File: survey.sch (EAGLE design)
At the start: 11 parts, among them IC1 DS1820, J1 PJ-102AH

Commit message: add receiver's shematic
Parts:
- renumbered IC1 to TSENSOR, J1 to SOCKET, JP1 to USB, U1 to ESP-12E
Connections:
- net GND: now also ESP-12E.GPIO0, ESP-12E.GPIO15
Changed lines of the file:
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@@
 </classes>
 <parts>
-<part name="U1" library="esp8266modules" deviceset="ESP12E" device="SMD"/>
-<part name="IC1" library="DS1820" deviceset="DS1820" device=""/>
+<part name="ESP-12E" library="esp8266modules" deviceset="ESP12E" device="SMD"/>
+<part name="TSENSOR" library="DS1820" deviceset="DS1820" device=""/>
 <part name="GND1" library="supply1" library_urn="urn:adsk.eagle:library:371" deviceset="GND" device=""/>
 <part name="SUPPLY1" library="supply2" library_urn="urn:adsk.eagle:library:372" deviceset="VCC" device=""/>
-<part name="JP1" library="pinhead" library_urn="urn:adsk.eagle:library:325" deviceset="PINHD-1X4" device="" package3d_urn="urn:adsk.eagle:package:22407/2"/>
+<part name="USB" library="pinhead" library_urn="urn:adsk.eagle:library:325" deviceset="PINHD-1X4" device="" package3d_urn="urn:adsk.eagle:package:22407/2"/>
 <part name="SUPPLY2" library="supply2" library_urn="urn:adsk.eagle:library:372" deviceset="VCC" device=""/>
 <part name="GND2" library="supply1" library_urn="urn:adsk.eagle:library:371" deviceset="GND" device=""/>
 <part name="GND3" library="supply1" library_urn="urn:adsk.eagle:library:371" deviceset="GND" device=""/>
-<part name="J1" library="connector" deviceset="PJ-102AH" device=""/>
+<part name="SOCKET" library="connector" deviceset="PJ-102AH" device=""/>
 <part name="GND4" library="supply1" library_urn="urn:adsk.eagle:library:371" deviceset="GND" device=""/>
 <part name="C1" library="rcl" library_urn="urn:adsk.eagle:library:334" deviceset="CPOL-EU" device="E2.5-6" package3d_urn="urn:adsk.eagle:package:23349/1"/>
@@
 <part name="H3" library="holes" library_urn="urn:adsk.eagle:library:237" deviceset="MOUNT-HOLE" device="3.0" package3d_urn="urn:adsk.eagle:package:14277/1"/>
 <part name="H4" library="holes" library_urn="urn:adsk.eagle:library:237" deviceset="MOUNT-HOLE" device="3.0" package3d_urn="urn:adsk.eagle:package:14277/1"/>
+<part name="GND6" library="supply1" library_urn="urn:adsk.eagle:library:371" deviceset="GND" device=""/>
+<part name="GND7" library="supply1" library_urn="urn:adsk.eagle:library:371" deviceset="GND" device=""/>
 </parts>
 <sheets>
@@
 </plain>
 <instances>
-<instance part="U1" gate="G$1" x="55.88" y="78.74"/>
-<instance part="IC1" gate="G$1" x="116.84" y="83.82"/>
+<instance part="ESP-12E" gate="G$1" x="55.88" y="78.74"/>
+<instance part="TSENSOR" gate="G$1" x="116.84" y="83.82"/>
 <instance part="GND1" gate="1" x="116.84" y="71.12"/>
 <instance part="SUPPLY1" gate="G$1" x="96.52" y="88.9"/>
-<instance part="JP1" gate="A" x="88.9" y="96.52"/>
+<instance part="USB" gate="A" x="88.9" y="96.52"/>
 <instance part="SUPPLY2" gate="G$1" x="76.2" y="106.68"/>
 <instance part="GND2" gate="1" x="78.74" y="88.9"/>
 <instance part="GND3" gate="1" x="78.74" y="66.04"/>
-<instance part="J1" gate="G$1" x="-2.54" y="109.22"/>
+<instance part="SOCKET" gate="G$1" x="-2.54" y="109.22"/>
 <instance part="GND4" gate="1" x="7.62" y="101.6"/>
 <instance part="C1" gate="G$1" x="15.24" y="109.22"/>
@@
 <instance part="H3" gate="G$1" x="111.76" y="114.3"/>
 <instance part="H4" gate="G$1" x="99.06" y="114.3"/>
+<instance part="GND6" gate="1" x="83.82" y="76.2"/>
+<instance part="GND7" gate="1" x="88.9" y="63.5"/>
 </instances>
 <busses>
@@
 <net name="N$1" class="0">
 <segment>
-<pinref part="IC1" gate="G$1" pin="DQ"/>
+<pinref part="TSENSOR" gate="G$1" pin="DQ"/>
 <wire x1="127" y1="86.36" x2="127" y2="66.04" width="0.1524" layer="91"/>
-<pinref part="U1" gate="G$1" pin="GPIO2"/>
+<pinref part="ESP-12E" gate="G$1" pin="GPIO2"/>
 <wire x1="71.12" y1="73.66" x2="96.52" y2="73.66" width="0.1524" layer="91"/>
 <wire x1="96.52" y1="73.66" x2="96.52" y2="66.04" width="0.1524" layer="91"/>
@@
 <segment>
 <pinref part="SUPPLY1" gate="G$1" pin="VCC"/>
-<pinref part="IC1" gate="G$1" pin="VDD"/>
+<pinref part="TSENSOR" gate="G$1" pin="VDD"/>
 <wire x1="96.52" y1="86.36" x2="106.68" y2="86.36" width="0.1524" layer="91"/>
 </segment>
 <segment>
-<pinref part="JP1" gate="A" pin="1"/>
+<pinref part="USB" gate="A" pin="1"/>
 <wire x1="86.36" y1="101.6" x2="76.2" y2="101.6" width="0.1524" layer="91"/>
 <wire x1="76.2" y1="101.6" x2="76.2" y2="104.14" width="0.1524" layer="91"/>
@@
 </segment>
 <segment>
-<pinref part="J1" gate="G$1" pin="VCC"/>
+<pinref part="SOCKET" gate="G$1" pin="VCC"/>
 <wire x1="5.08" y1="111.76" x2="15.24" y2="111.76" width="0.1524" layer="91"/>
 <pinref part="C1" gate="G$1" pin="+"/>
@@
 <segment>
 <pinref part="SUPPLY4" gate="G$1" pin="VCC"/>
-<pinref part="U1" gate="G$1" pin="VCC"/>
+<pinref part="ESP-12E" gate="G$1" pin="VCC"/>
 <wire x1="22.86" y1="68.58" x2="38.1" y2="68.58" width="0.1524" layer="91"/>
 </segment>
@@
 <segment>
 <pinref part="GND1" gate="1" pin="GND"/>
-<pinref part="IC1" gate="G$1" pin="GND"/>
+<pinref part="TSENSOR" gate="G$1" pin="GND"/>
 <wire x1="116.84" y1="73.66" x2="116.84" y2="76.2" width="0.1524" layer="91"/>
 </segment>
 <segment>
-<pinref part="JP1" gate="A" pin="4"/>
+<pinref part="USB" gate="A" pin="4"/>
 <wire x1="86.36" y1="93.98" x2="78.74" y2="93.98" width="0.1524" layer="91"/>
 <wire x1="78.74" y1="93.98" x2="78.74" y2="91.44" width="0.1524" layer="91"/>
@@
 </segment>
 <segment>
-<pinref part="U1" gate="G$1" pin="GND"/>
+<pinref part="ESP-12E" gate="G$1" pin="GND"/>
 <pinref part="GND3" gate="1" pin="GND"/>
 <wire x1="71.12" y1="68.58" x2="78.74" y2="68.58" width="0.1524" layer="91"/>
 </segment>
 <segment>
-<pinref part="J1" gate="G$1" pin="GND"/>
+<pinref part="SOCKET" gate="G$1" pin="GND"/>
 <wire x1="5.08" y1="106.68" x2="7.62" y2="106.68" width="0.1524" layer="91"/>
 <pinref part="GND4" gate="1" pin="GND"/>
@@
 <pinref part="GND5" gate="1" pin="GND"/>
 </segment>
+<segment>
+<pinref part="ESP-12E" gate="G$1" pin="GPIO0"/>
+<wire x1="71.12" y1="76.2" x2="78.74" y2="76.2" width="0.1524" layer="91"/>
+<wire x1="78.74" y1="76.2" x2="78.74" y2="81.28" width="0.1524" layer="91"/>
+<wire x1="78.74" y1="81.28" x2="83.82" y2="81.28" width="0.1524" layer="91"/>
+<pinref part="GND6" gate="1" pin="GND"/>
+<wire x1="83.82" y1="81.28" x2="83.82" y2="78.74" width="0.1524" layer="91"/>
+</segment>
+<segment>
+<pinref part="GND7" gate="1" pin="GND"/>
+<wire x1="88.9" y1="66.04" x2="88.9" y2="71.12" width="0.1524" layer="91"/>
+<pinref part="ESP-12E" gate="G$1" pin="GPIO15"/>
+<wire x1="88.9" y1="71.12" x2="71.12" y2="71.12" width="0.1524" layer="91"/>
+</segment>
 </net>
 <net name="N$3" class="0">
 <segment>
-<pinref part="U1" gate="G$1" pin="TX"/>
+<pinref part="ESP-12E" gate="G$1" pin="TX"/>
 <wire x1="71.12" y1="86.36" x2="73.66" y2="86.36" width="0.1524" layer="91"/>
 <wire x1="73.66" y1="86.36" x2="73.66" y2="99.06" width="0.1524" layer="91"/>
-<pinref part="JP1" gate="A" pin="2"/>
+<pinref part="USB" gate="A" pin="2"/>
 <wire x1="73.66" y1="99.06" x2="86.36" y2="99.06" width="0.1524" layer="91"/>
 </segment>
@@
 <net name="N$4" class="0">
 <segment>
-<pinref part="U1" gate="G$1" pin="RX"/>
+<pinref part="ESP-12E" gate="G$1" pin="RX"/>
 <wire x1="71.12" y1="83.82" x2="76.2" y2="83.82" width="0.1524" layer="91"/>
 <wire x1="76.2" y1="83.82" x2="76.2" y2="96.52" width="0.1524" layer="91"/>
-<pinref part="JP1" gate="A" pin="3"/>
+<pinref part="USB" gate="A" pin="3"/>
 <wire x1="76.2" y1="96.52" x2="86.36" y2="96.52" width="0.1524" layer="91"/>
 </segment>
@@
 <wire x1="30.48" y1="81.28" x2="33.02" y2="81.28" width="0.1524" layer="91"/>
 <wire x1="33.02" y1="81.28" x2="33.02" y2="86.36" width="0.1524" layer="91"/>
-<pinref part="U1" gate="G$1" pin="RESET"/>
+<pinref part="ESP-12E" gate="G$1" pin="RESET"/>
 <wire x1="33.02" y1="86.36" x2="38.1" y2="86.36" width="0.1524" layer="91"/>
-<pinref part="U1" gate="G$1" pin="CH_PD"/>
+<pinref part="ESP-12E" gate="G$1" pin="CH_PD"/>
 <wire x1="33.02" y1="81.28" x2="38.1" y2="81.28" width="0.1524" layer="91"/>
 <junction x="33.02" y="81.28"/>

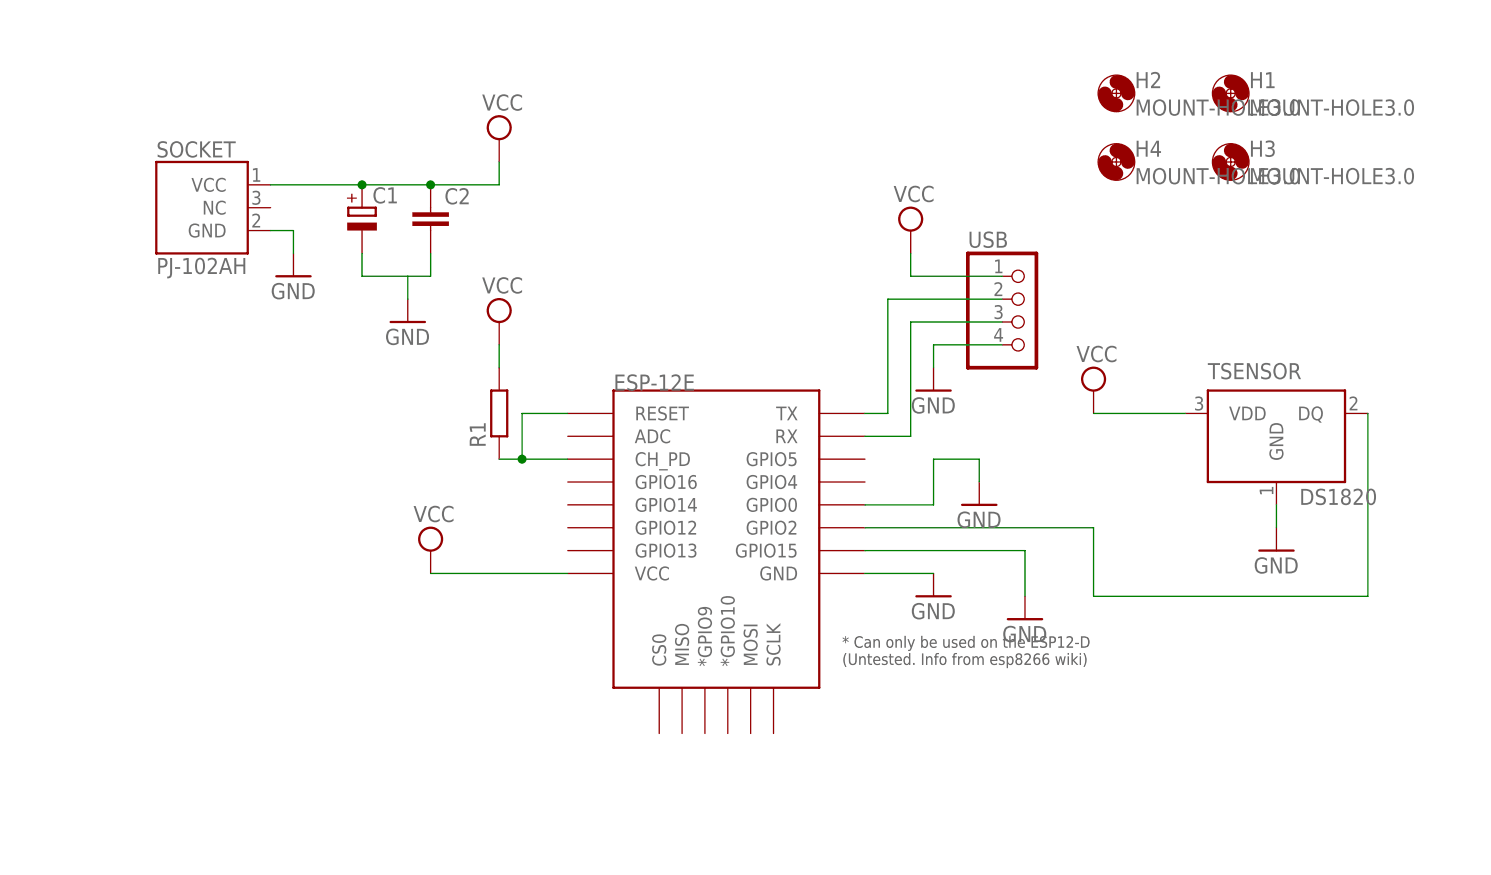
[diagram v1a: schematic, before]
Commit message: Improved some bugs in receiver's and survey's schematic.
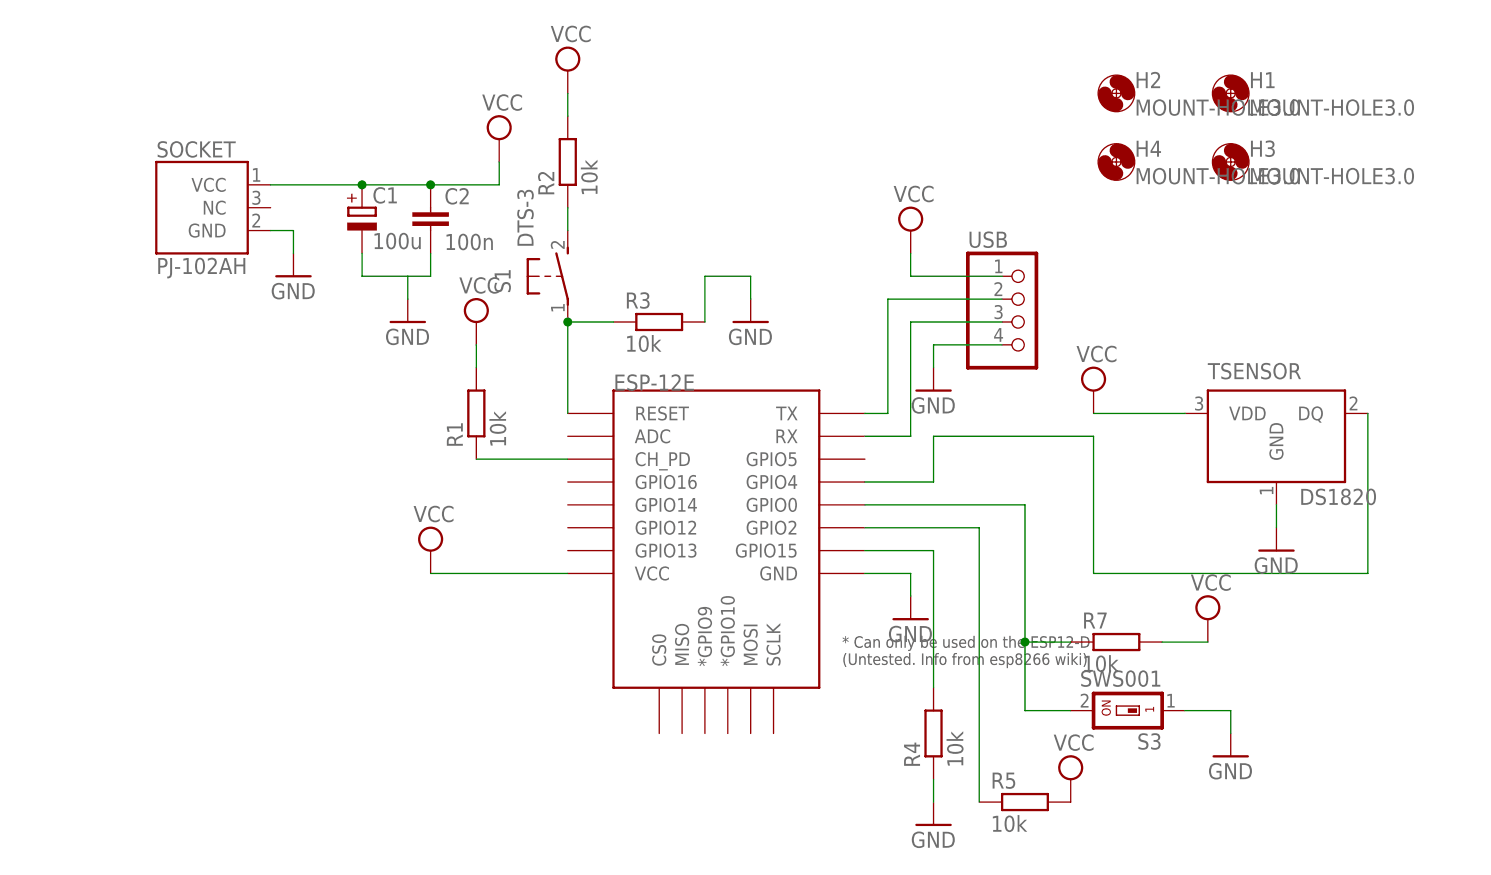
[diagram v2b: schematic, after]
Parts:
- added R2, R3, R4: 10k, rcl:R-EU_0204/7
- added R5, R7: 10k, rcl:R-EU_0204/5
- added S1: DTS-3, switch-tact:DTS-3
- added S3: SWS001, smd-special:SWS001
- C1: value (none) -> 100u
- C2: value (none) -> 100n
- R1: value (none) -> 10k
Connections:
- new net N$10: ESP-12E.RESET, R3.1, S1.1
- new net N$11: R2.1, S1.2
- new net N$5: ESP-12E.GPIO4, TSENSOR.DQ
- new net N$6: R7.1, S3.2
- new net N$7: ESP-12E.GPIO15, R4.2
- net GND: now also R3.2, R4.1, S3.1; no longer ESP-12E.GND, ESP-12E.GPIO0, ESP-12E.GPIO15
- net N$1: now also R5.1; no longer ESP-12E.GPIO2, TSENSOR.DQ
- net N$2: no longer ESP-12E.RESET
- net VCC: now also R2.2, R5.2, R7.2
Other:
- moved on the sheet: R1

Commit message: Corrected reset pin connection and added pull-up resistor to temperature sensor.
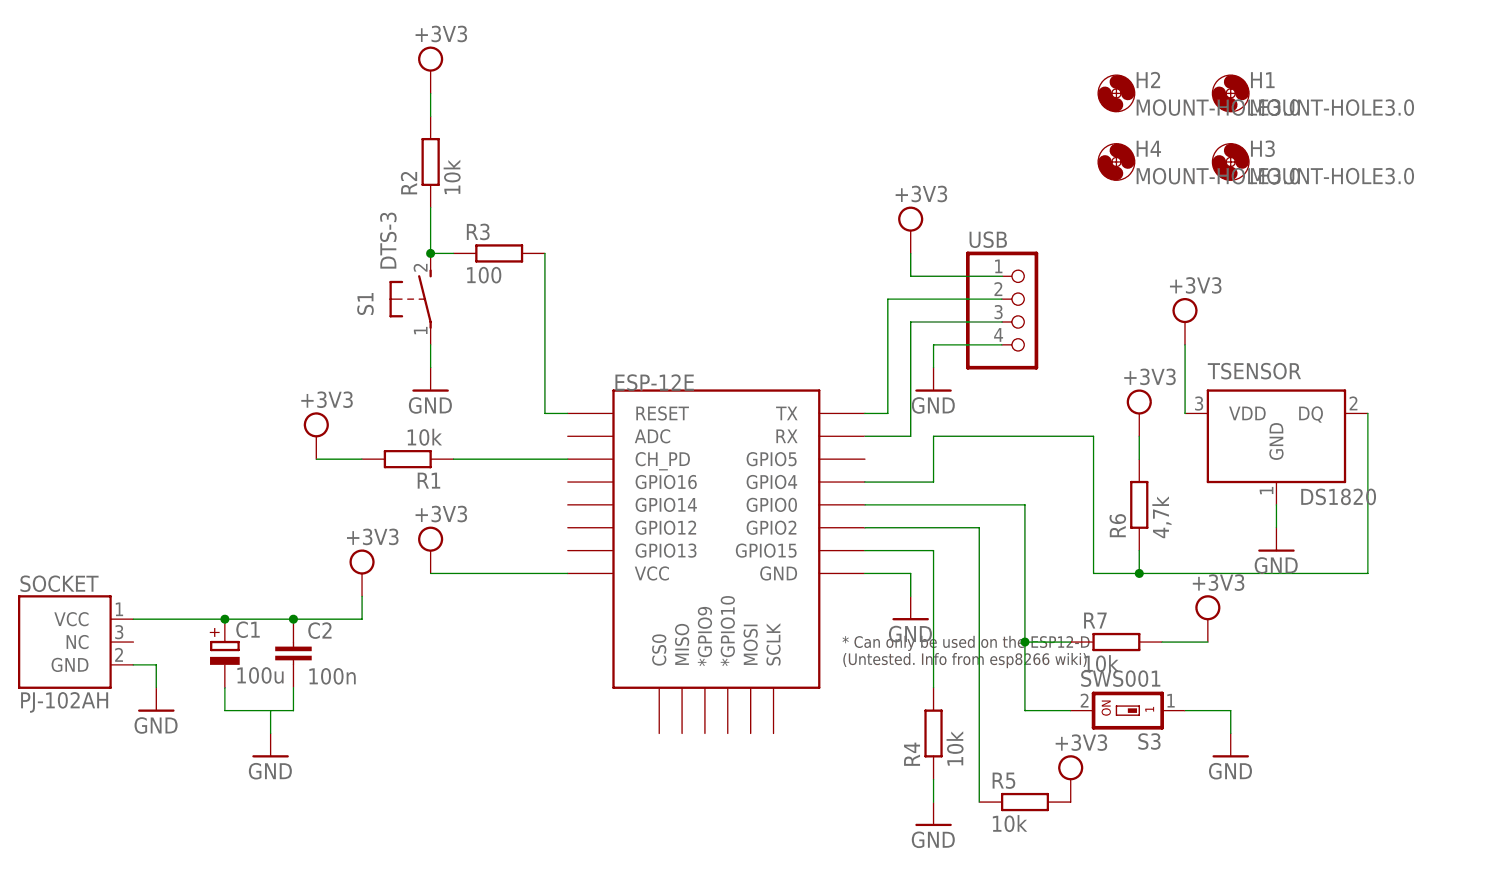
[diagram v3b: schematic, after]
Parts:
- added R6: 4,7k, rcl:R-EU_0204/7
- R3: value 10k -> 100
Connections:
- removed net N$10: ESP-12E.RESET, R3.1, S1.1
- removed net N$11: R2.1, S1.2
- new net N$8: R2.1, R3.1, S1.2
- new net N$9: ESP-12E.RESET, R3.2
- net GND: now also S1.1; no longer R3.2
- net N$5: now also R6.1
- net VCC: now also R6.2
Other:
- moved on the sheet: C1, C2, R1, R2, R3, S1, SOCKET

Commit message: Changed some resistors from 10k for 2k2 and added resisors 100 to reset and gpio0 pin.
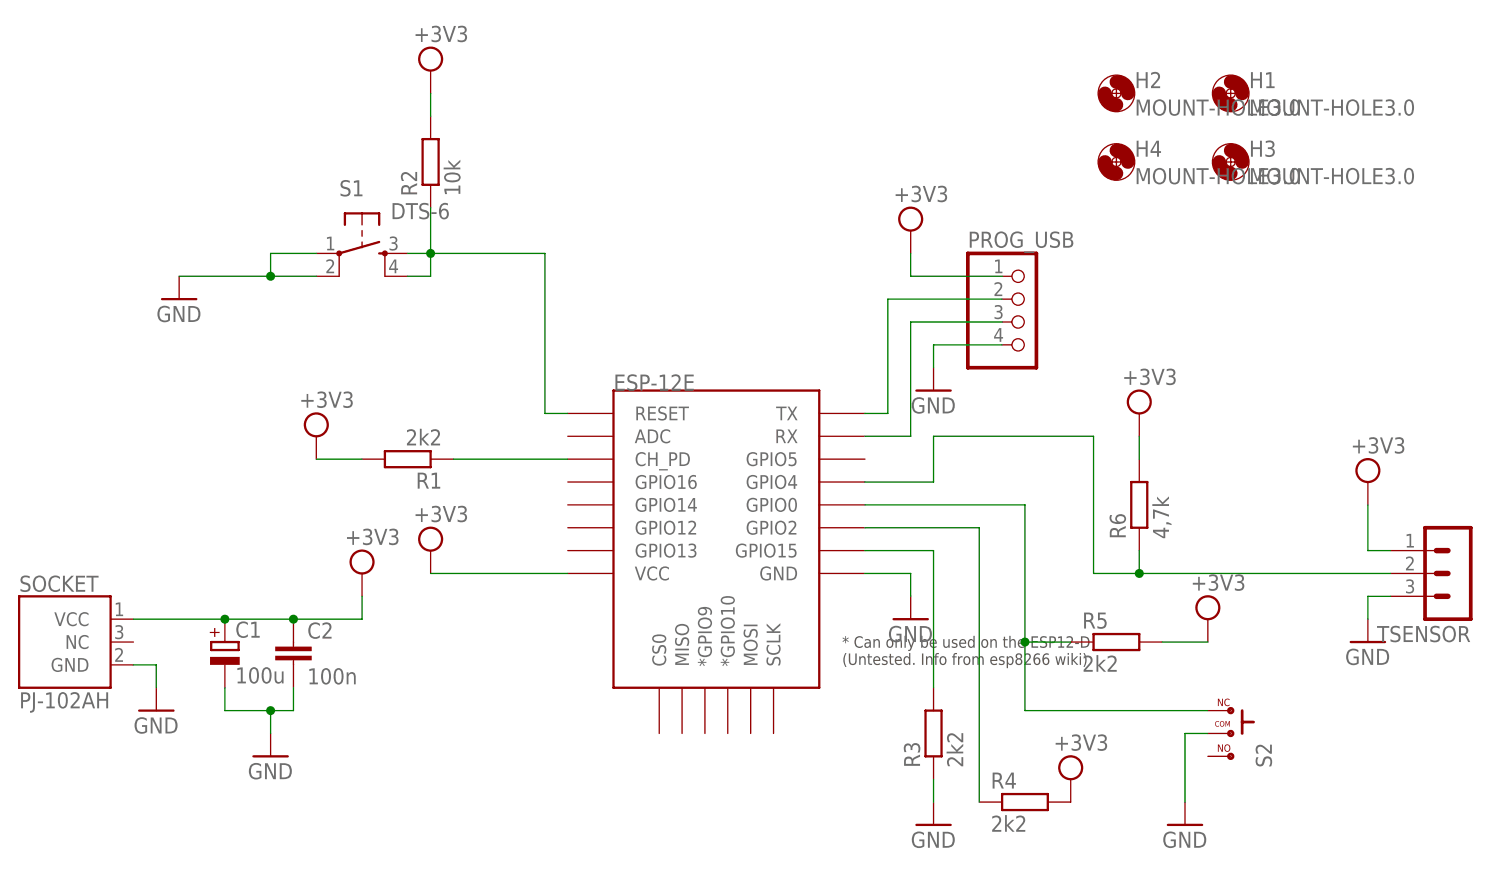
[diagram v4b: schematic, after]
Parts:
- removed R7: 10k, rcl:R-EU_0204/5
- removed S3: SWS001, smd-special:SWS001
- added S2: -SWITCH, tango:-SWITCH
- R1, R4: value 10k -> 2k2
- R3: value 100 -> 2k2
- R5: value 10k -> 2k2; device rcl:R-EU_0204/5 -> rcl:R-EU_0204/7
- S1: value DTS-3 -> DTS-6; device switch-tact:DTS-3 -> switch-tact:DTS-6
- TSENSOR: value DS1820 -> (none); device DS1820:DS1820 -> con-lstb:MA03-1
- renumbered USB to PROG_USB
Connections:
- removed net N$9: ESP-12E.RESET, R3.2
- net GND: now also R3.1, S1.2, S2.2, TSENSOR.3; no longer R4.1, S3.1, TSENSOR.GND
- net N$1: now also ESP-12E.GPIO2, R4.1; no longer R5.1
- net N$5: now also TSENSOR.2; no longer TSENSOR.DQ
- net N$6: now also ESP-12E.GPIO0, R5.1, S2.1; no longer R7.1, S3.2
- net N$7: now also R3.2; no longer R4.2
- net N$8: now also ESP-12E.RESET, S1.3, S1.4; no longer R3.1, S1.2
- net VCC: now also R4.2, TSENSOR.1; no longer R7.2, TSENSOR.VDD
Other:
- moved on the sheet: R3, R4, R5, TSENSOR
